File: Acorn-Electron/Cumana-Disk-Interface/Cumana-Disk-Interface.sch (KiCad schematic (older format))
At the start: 55 parts, among them J1 18 finger Edge Connector, J2 24 finger Edge Connector, J3 34-way IDC header, Q2 BC337, Q3 BC337, Q4 BC327, Q5 BC337, U1 74LS138, U10 74LS174, U11 M5W1793-02P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

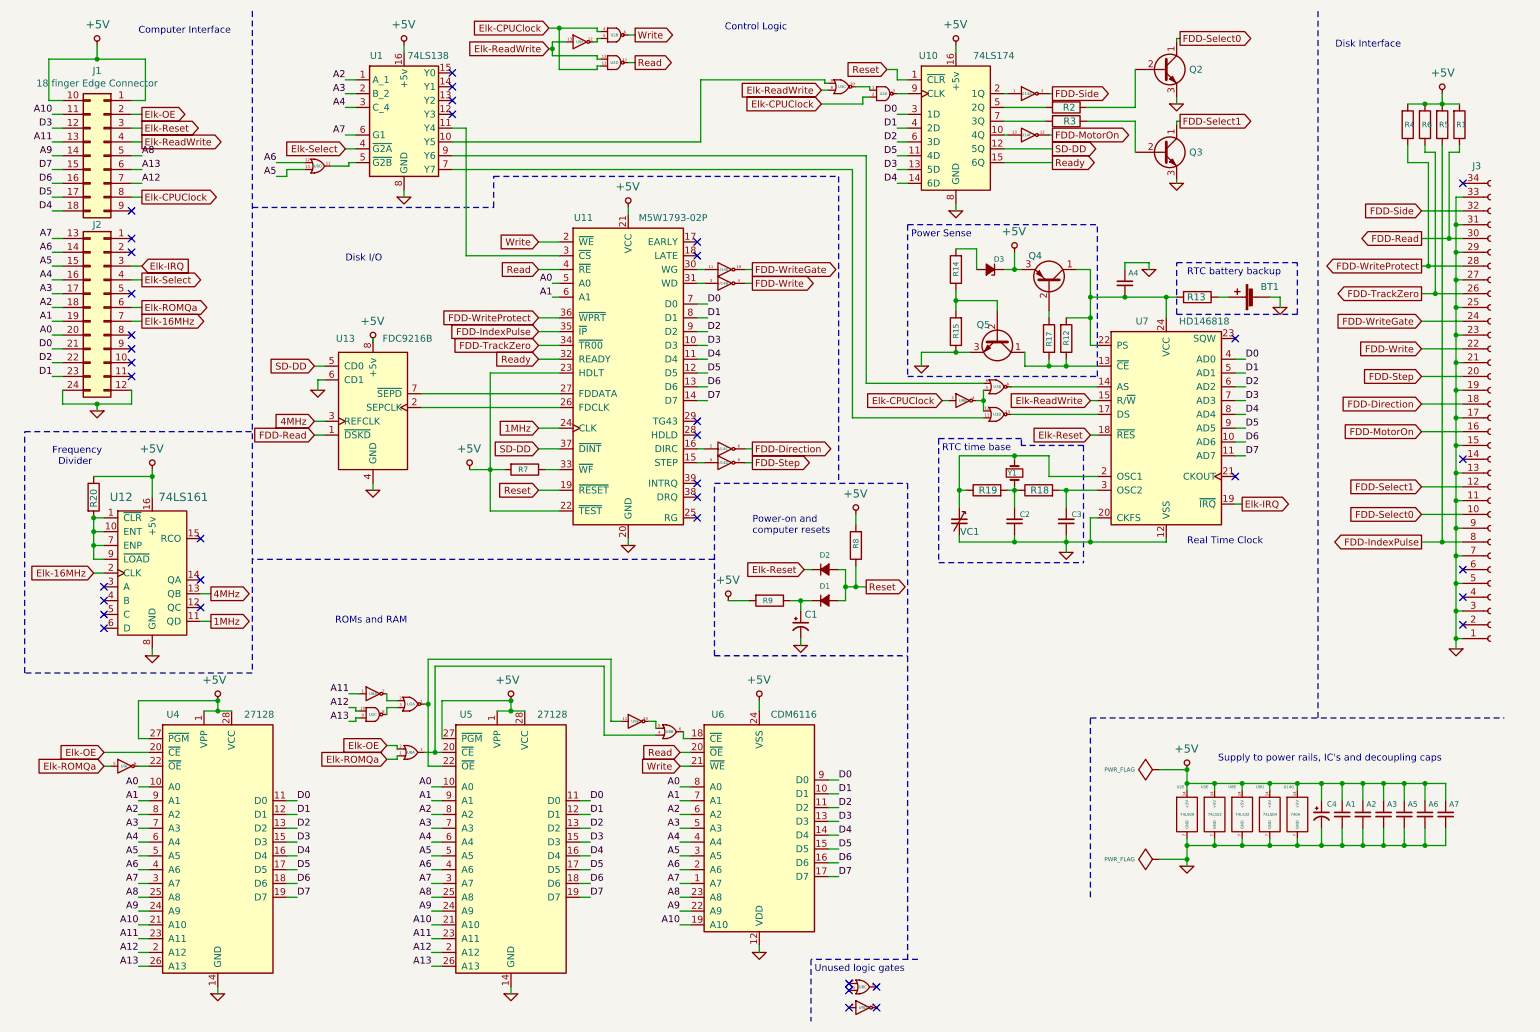
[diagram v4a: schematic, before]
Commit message: show values for caps and resistors
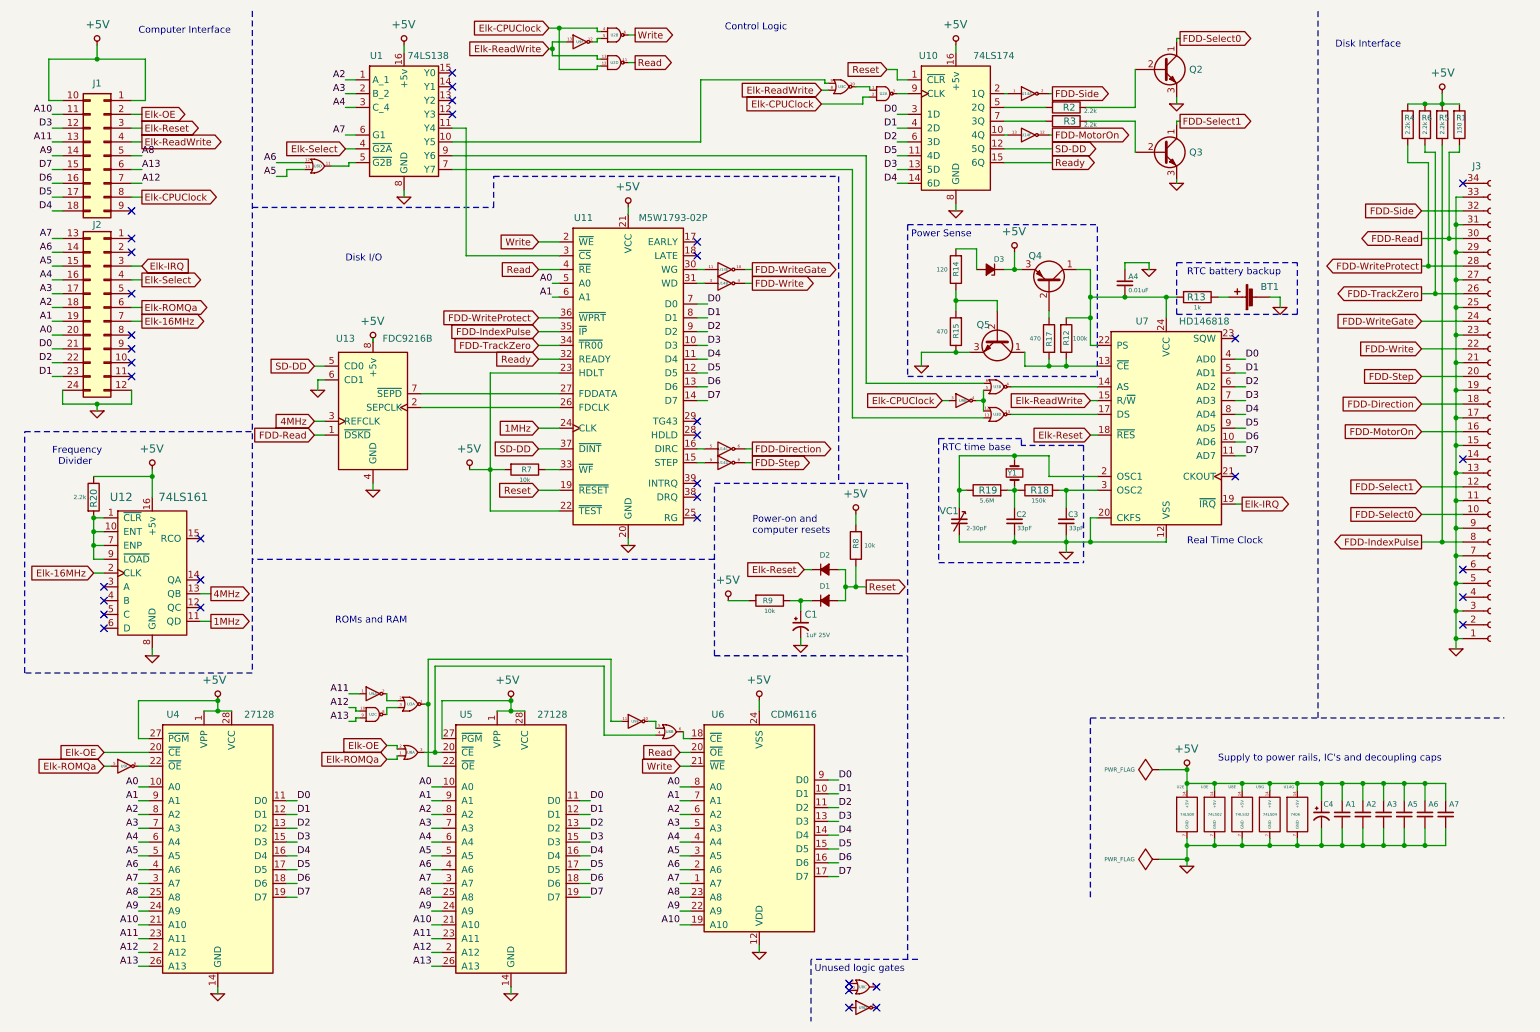
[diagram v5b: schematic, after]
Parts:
- VC1: value 2 - 30pF -> 2-30pF
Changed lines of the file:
@@
 U 1 1 647FD16F
 P 10775 1300
-F 0 "R5" H 10825 1300 40  0000 R CNN
-F 1 "2.2k" V 10675 1300 40  0001 C CNN
+F 0 "R5" H 10825 1250 40  0000 R CNN
+F 1 "2.2k" V 10775 1325 31  0000 C CNN
 F 2 "Cumana-Disk-Interface:R_Axial_DIN0212_L12.5mm_D2.5mm_Horizontal" V 10705 1300 30  0001 C CNN
 F 3 "" H 10775 1250 30  0000 C CNN
@@
 U 1 1 64807553
 P 10525 1300
-F 0 "R4" H 10575 1300 40  0000 R CNN
-F 1 "2.2k" V 10425 1300 40  0001 C CNN
+F 0 "R4" H 10575 1250 40  0000 R CNN
+F 1 "2.2k" V 10525 1325 31  0000 C CNN
 F 2 "Cumana-Disk-Interface:R_Axial_DIN0212_L12.5mm_D2.5mm_Horizontal" V 10455 1300 30  0001 C CNN
 F 3 "" H 10525 1250 30  0000 C CNN
@@
 U 1 1 648078C1
 P 10650 1300
-F 0 "R6" H 10700 1300 40  0000 R CNN
-F 1 "2.2k" V 10550 1300 40  0001 C CNN
+F 0 "R6" H 10700 1250 40  0000 R CNN
+F 1 "2.2k" V 10650 1325 31  0000 C CNN
 F 2 "Cumana-Disk-Interface:R_Axial_DIN0212_L12.5mm_D2.5mm_Horizontal" V 10580 1300 30  0001 C CNN
 F 3 "" H 10650 1250 30  0000 C CNN
@@
 U 1 1 64811A22
 P 4125 3800
-F 0 "R7" V 4125 3825 40  0000 R CNN
-F 1 "10k" V 4025 3800 40  0001 C CNN
+F 0 "R7" V 4125 3850 40  0000 R CNN
+F 1 "10k" V 4200 3800 31  0000 C CNN
 F 2 "Cumana-Disk-Interface:R_Axial_DIN0212_L12.5mm_D2.5mm_Horizontal" V 4055 3800 30  0001 C CNN
 F 3 "" H 4125 3750 30  0000 C CNN
@@
 U 1 1 6483E2A3
 P 1075 1525
-F 0 "J1" H 1125 2142 50  0000 C CNN
-F 1 "18 finger Edge Connector" H 1125 2050 50  0000 C CNN
+F 0 "J1" H 1125 2050 50  0000 C CNN
+F 1 "18 finger Edge Connector" H 1125 2050 50  0001 C CNN
 F 2 "Cumana-Disk-Interface:Connector_2x9_P1.27mm_Polarized_Edge" H 1075 1525 50  0001 C CNN
 F 3 "" H 1075 1525 50  0001 C CNN
@@
 P 8050 1175
 F 0 "R2" V 8050 1150 50  0000 L CNN
-F 1 "2.2k" V 7950 1175 50  0001 C CNN
+F 1 "2.2k" V 8075 1350 31  0000 C CNN
 F 2 "Cumana-Disk-Interface:R_Axial_DIN0212_L12.5mm_D2.5mm_Horizontal" V 7980 1175 50  0001 C CNN
 F 3 "" H 8050 1175 50  0001 C CNN
@@
 P 8050 1275
 F 0 "R3" V 8050 1300 50  0000 C CNN
-F 1 "2.2k" V 7950 1275 50  0001 C CNN
+F 1 "2.2k" V 8075 1450 31  0000 C CNN
 F 2 "Cumana-Disk-Interface:R_Axial_DIN0212_L12.5mm_D2.5mm_Horizontal" V 7980 1275 50  0001 C CNN
 F 3 "" H 8050 1275 50  0001 C CNN
@@
 P 1000 4000
 F 0 "R20" V 1000 3925 50  0000 L CNN
-F 1 "2.2k" V 900 4000 50  0001 C CNN
+F 1 "2.2k" H 900 4000 31  0000 C CNN
 F 2 "Cumana-Disk-Interface:R_Axial_DIN0212_L12.5mm_D2.5mm_Horizontal" V 930 4000 50  0001 C CNN
 F 3 "" H 1000 4000 50  0001 C CNN
@@
 U 1 1 652545DF
 P 10900 1300
-F 0 "R1" H 10950 1300 40  0000 R CNN
-F 1 "150" V 10800 1300 40  0001 C CNN
+F 0 "R1" H 10950 1250 40  0000 R CNN
+F 1 "150" V 10900 1325 31  0000 C CNN
 F 2 "Cumana-Disk-Interface:R_Axial_DIN0212_L12.5mm_D2.5mm_Horizontal" V 10830 1300 30  0001 C CNN
 F 3 "" H 10900 1250 30  0000 C CNN
@@
 P 5900 4750
 F 0 "R9" V 5900 4700 40  0000 L CNN
-F 1 "10k" V 5800 4750 40  0001 C CNN
+F 1 "10k" V 5975 4750 31  0000 C CNN
 F 2 "Cumana-Disk-Interface:R_Axial_DIN0212_L12.5mm_D2.5mm_Horizontal" V 5830 4750 30  0001 C CNN
 F 3 "" H 5900 4700 30  0000 C CNN
@@
 P 6125 4925
 F 0 "C1" H 6200 5000 50  0000 C CNN
-F 1 "1uF 25V" V 5946 4925 50  0001 C CNN
+F 1 "1uF 25V" H 6250 4850 31  0000 C CNN
 F 2 "Cumana-Disk-Interface:CP_Radial_Tantal_D4.5mm_P5.00mm" H 6125 4925 60  0001 C CNN
 F 3 "" H 6125 4925 60  0000 C CNN
@@
 P 6525 4350
 F 0 "R8" V 6525 4300 40  0000 L CNN
-F 1 "10k" V 6425 4350 40  0001 C CNN
+F 1 "10k" H 6425 4350 31  0000 C CNN
 F 2 "Cumana-Disk-Interface:R_Axial_DIN0212_L12.5mm_D2.5mm_Horizontal" V 6455 4350 30  0001 C CNN
 F 3 "" H 6525 4300 30  0000 C CNN
@@
 P 7925 2850
 F 0 "R17" V 7925 2900 40  0000 R CNN
-F 1 "470" V 7825 2850 40  0001 C CNN
+F 1 "470" H 8025 2850 31  0000 C CNN
 F 2 "Cumana-Disk-Interface:R_Axial_DIN0212_L12.5mm_D2.5mm_Horizontal" V 7855 2850 30  0001 C CNN
 F 3 "" H 7925 2800 30  0000 C CNN
@@
 P 8050 2850
 F 0 "R12" V 8050 2900 40  0000 R CNN
-F 1 "100k" V 7950 2850 40  0001 C CNN
+F 1 "100k" H 8150 2850 31  0000 C CNN
 F 2 "Cumana-Disk-Interface:R_Axial_DIN0212_L12.5mm_D2.5mm_Horizontal" V 7980 2850 30  0001 C CNN
 F 3 "" H 8050 2800 30  0000 C CNN
@@
 P 7250 2350
 F 0 "R14" V 7250 2400 40  0000 R CNN
-F 1 "120" V 7150 2350 40  0001 C CNN
+F 1 "120" H 7350 2350 31  0000 C CNN
 F 2 "Cumana-Disk-Interface:R_Axial_DIN0212_L12.5mm_D2.5mm_Horizontal" V 7180 2350 30  0001 C CNN
 F 3 "" H 7250 2300 30  0000 C CNN
@@
 P 7250 2800
 F 0 "R15" V 7250 2850 40  0000 R CNN
-F 1 "470" V 7150 2800 40  0001 C CNN
+F 1 "470" H 7350 2800 31  0000 C CNN
 F 2 "Cumana-Disk-Interface:R_Axial_DIN0212_L12.5mm_D2.5mm_Horizontal" V 7180 2800 30  0001 C CNN
 F 3 "" H 7250 2750 30  0000 C CNN
@@
 P 7850 3950
 F 0 "R18" V 7850 3875 50  0000 L CNN
-F 1 "150k" V 7750 3950 50  0001 C CNN
+F 1 "150k" V 7775 3950 31  0000 C CNN
 F 2 "Cumana-Disk-Interface:R_Axial_DIN0212_L12.5mm_D2.5mm_Horizontal" V 7780 3950 50  0001 C CNN
 F 3 "" H 7850 3950 50  0001 C CNN
@@
 P 7475 3950
 F 0 "R19" V 7475 3875 50  0000 L CNN
-F 1 "5.6M" V 7375 3950 50  0001 C CNN
+F 1 "5.6M" V 7400 3950 31  0000 C CNN
 F 2 "Cumana-Disk-Interface:R_Axial_DIN0212_L12.5mm_D2.5mm_Horizontal" V 7405 3950 50  0001 C CNN
 F 3 "" H 7475 3950 50  0001 C CNN
@@
 U 1 1 65051B24
 P 7275 4175
-F 0 "VC1" H 7350 4100 50  0000 C CNN
-F 1 "2 - 30pF" V 7114 4175 50  0001 C CNN
+F 0 "VC1" H 7200 4250 50  0000 C CNN
+F 1 "2-30pF" H 7400 4125 31  0000 C CNN
 F 2 "Cumana-Disk-Interface:C_Trimmer" H 7275 4175 50  0001 C CNN
 F 3 "" H 7275 4175 50  0001 C CNN
@@
 U 1 1 64C60711
 P 8050 4175
-F 0 "C3" H 7975 4125 40  0000 C CNN
-F 1 "33pF" H 8100 4125 40  0001 L CNN
+F 0 "C3" H 8000 4125 40  0000 C CNN
+F 1 "33pF" H 7925 4225 31  0000 L CNN
 F 2 "Cumana-Disk-Interface:C_Disc_D4.3mm_W1.9mm_P5.00mm" H 8088 4025 30  0001 C CNN
 F 3 "" H 8050 4175 60  0000 C CNN
@@
 U 1 1 67D78D69
 P 9900 6300
-F 0 "C4" H 9975 6375 39  0000 C CNN
-F 1 "10uF 6.3V" V 9721 6300 50  0001 C CNN
+F 0 "C4" H 9950 6375 39  0000 C CNN
+F 1 "10uF 6.3V" H 9975 6200 31  0001 C CNN
 F 2 "Cumana-Disk-Interface:CP_Radial_Tantal_D4.5mm_P5.00mm" H 9900 6300 60  0001 C CNN
 F 3 "" H 9900 6300 60  0000 C CNN
@@
 P 9000 2550
 F 0 "R13" V 9000 2475 50  0000 L CNN
-F 1 "1k" V 8900 2550 50  0001 C CNN
+F 1 "1k" V 9075 2550 31  0000 C CNN
 F 2 "Cumana-Disk-Interface:R_Axial_DIN0212_L12.5mm_D2.5mm_Horizontal" V 8930 2550 50  0001 C CNN
 F 3 "" H 9000 2550 50  0001 C CNN
@@
 U 1 1 6574202A
 P 8475 2450
-F 0 "A4" H 8500 2525 40  0000 L CNN
-F 1 "0.01uF" H 8525 2400 40  0001 L CNN
+F 0 "A4" H 8500 2500 40  0000 L CNN
+F 1 "0.01uF" H 8500 2400 31  0000 L CNN
 F 2 "Cumana-Disk-Interface:C_Disc_D8.0mm_W2.5mm_P5.00mm" H 8513 2300 30  0001 C CNN
 F 3 "" H 8475 2450 60  0000 C CNN
@@
 U 1 1 64C60A2A
 P 7675 4175
-F 0 "C2" H 7600 4125 40  0000 C CNN
-F 1 "33pF" H 7725 4125 40  0001 L CNN
+F 0 "C2" H 7625 4125 40  0000 C CNN
+F 1 "33pF" H 7550 4225 31  0000 L CNN
 F 2 "Cumana-Disk-Interface:C_Disc_D4.3mm_W1.9mm_P5.00mm" H 7713 4025 30  0001 C CNN
 F 3 "" H 7675 4175 60  0000 C CNN
